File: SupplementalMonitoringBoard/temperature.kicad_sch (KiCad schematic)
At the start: 11 parts, among them U3 INA180B1

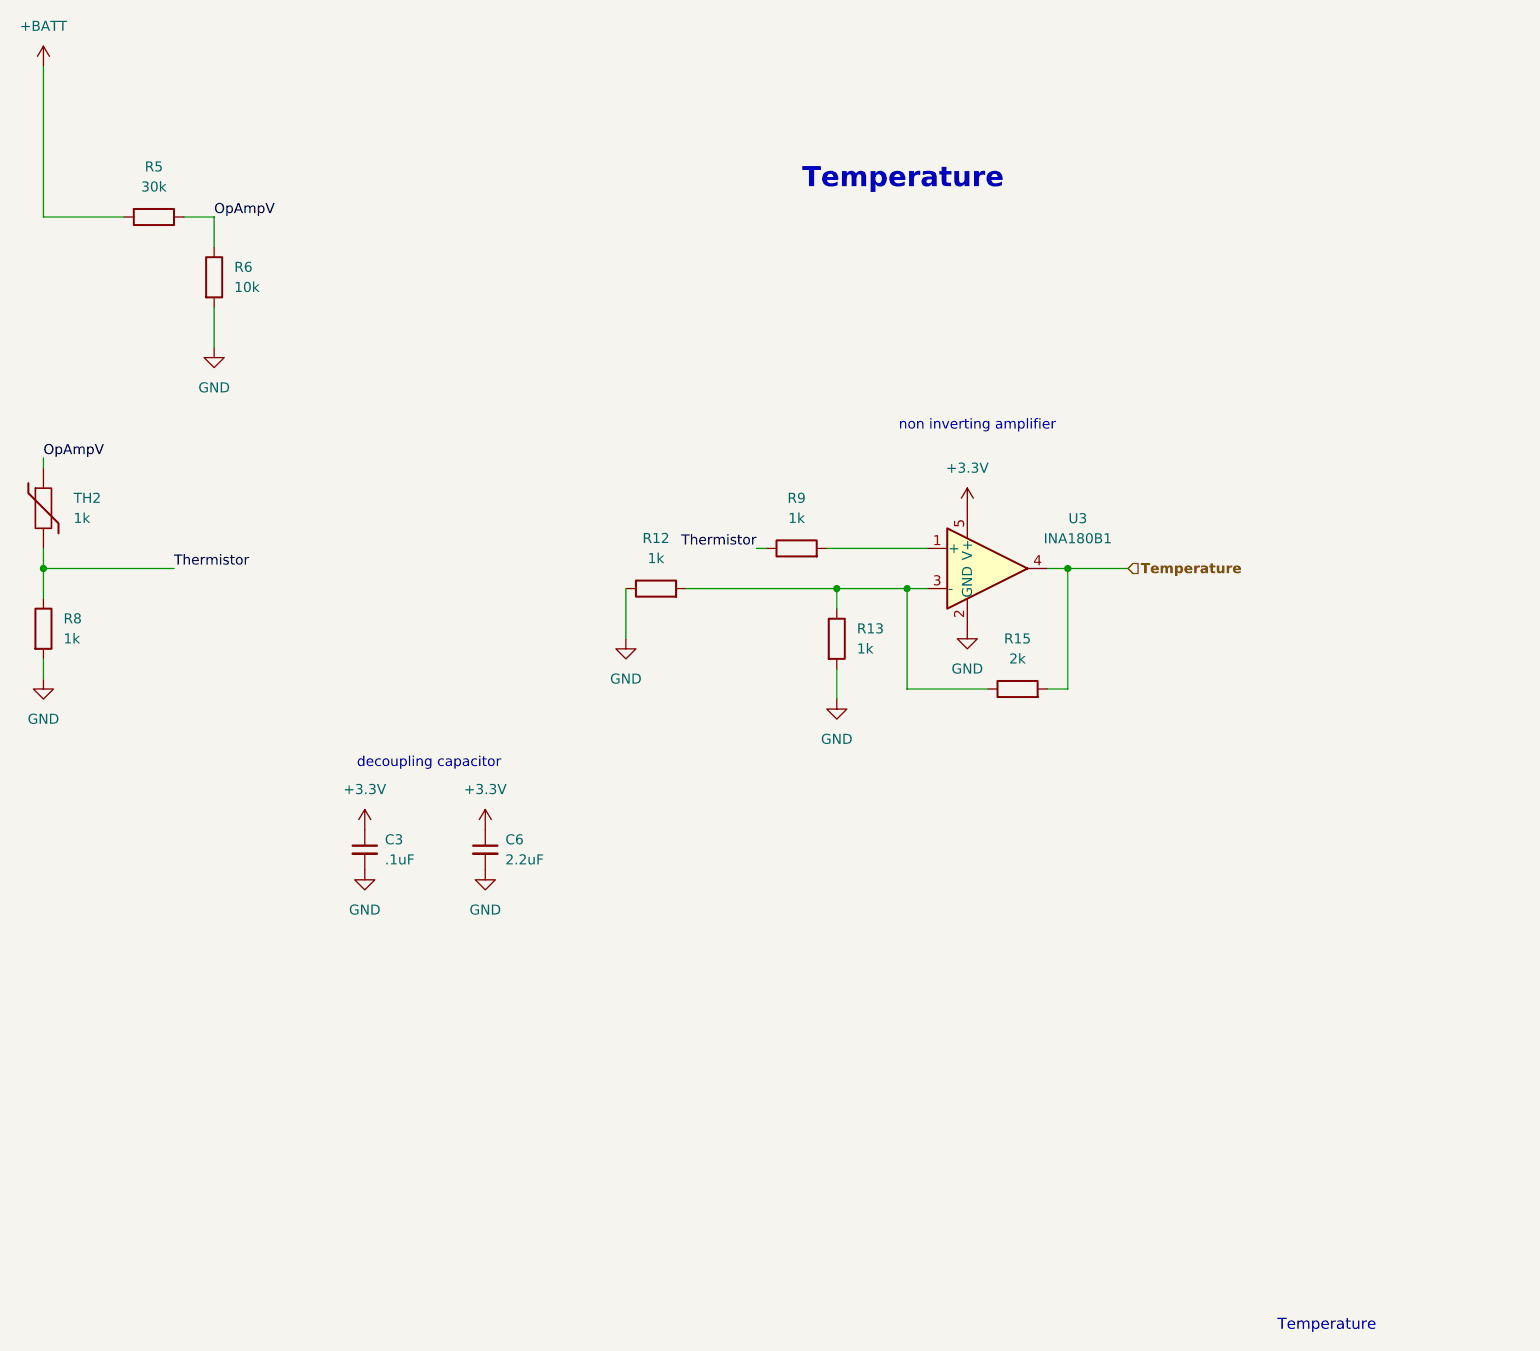
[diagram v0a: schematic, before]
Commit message: Supplemental Monitoring Board
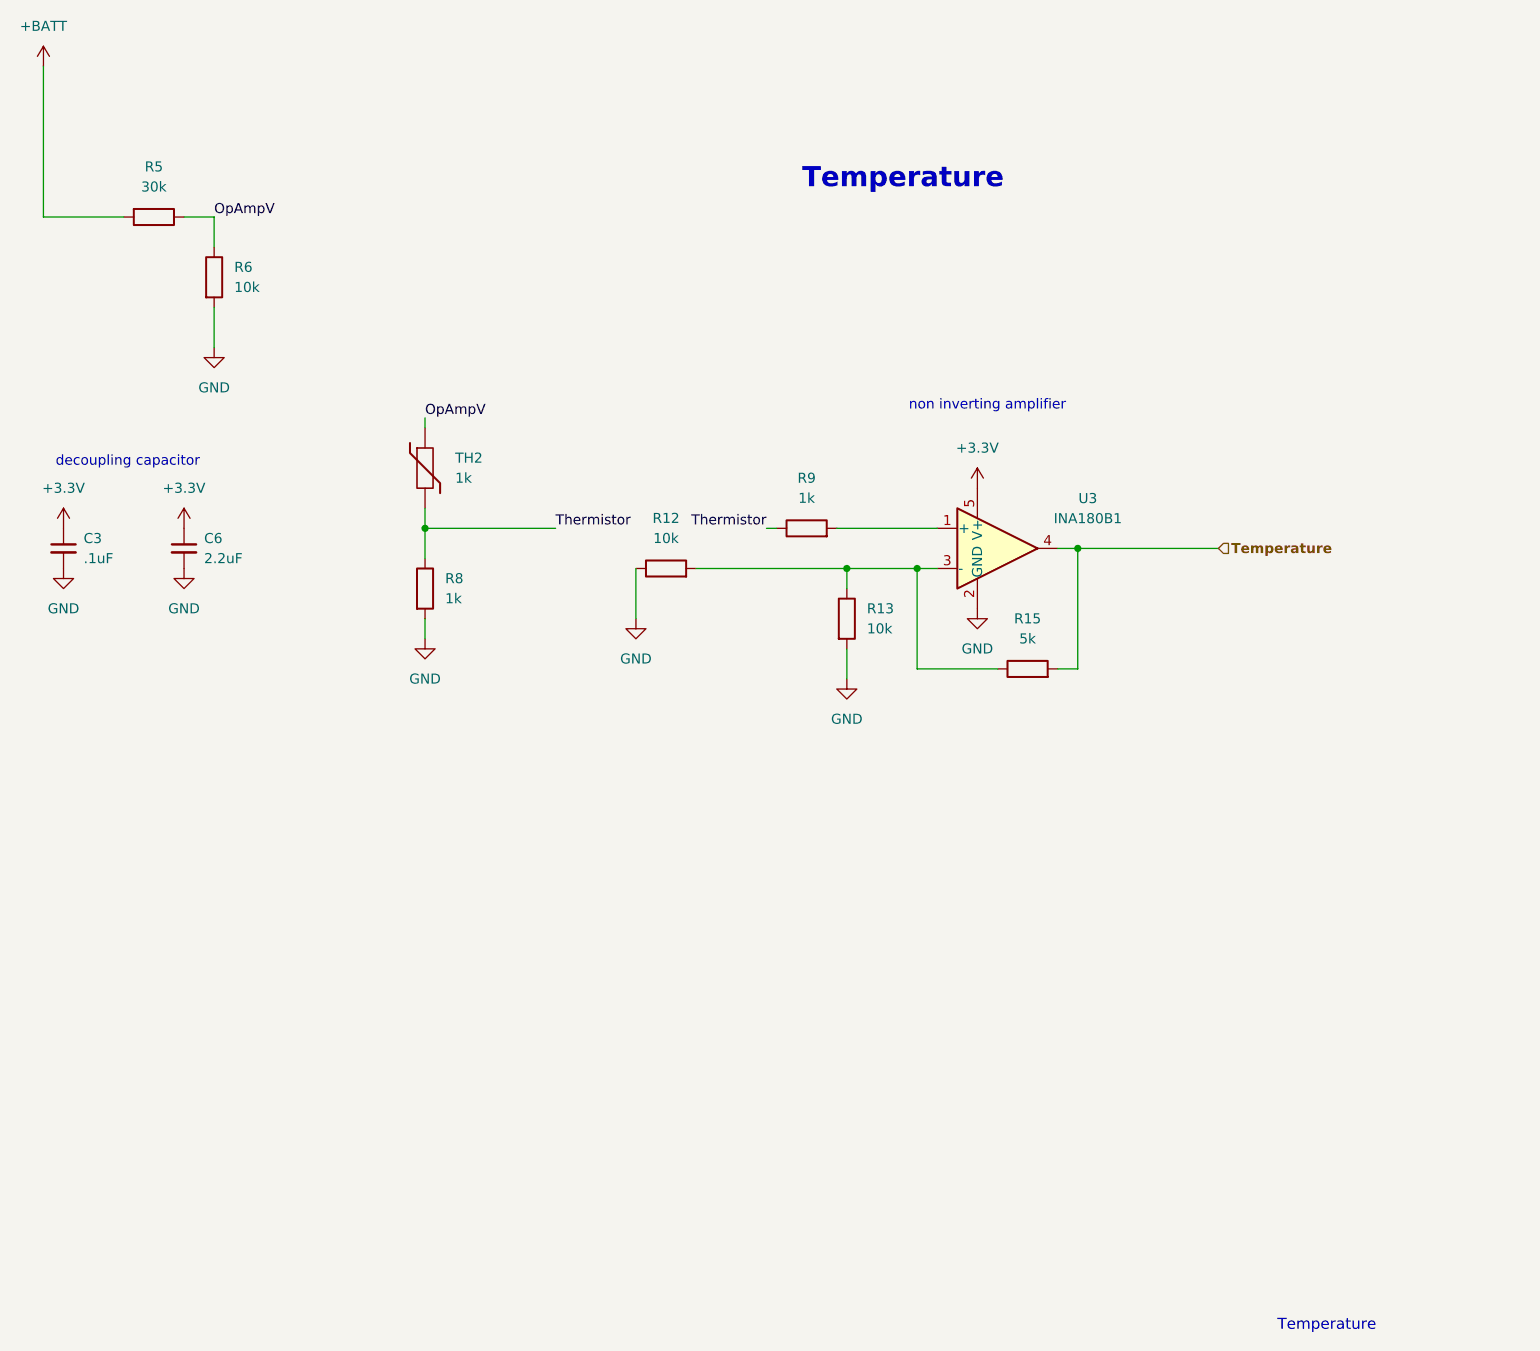
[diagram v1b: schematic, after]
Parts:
- R12, R13: value 1k -> 10k
- R15: value 2k -> 5k
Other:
- moved on the sheet: C3, C6, R12, R13, R15, R8, R9, TH2, U3

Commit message: Adressed Reviews - Supplemental Monitoring Board
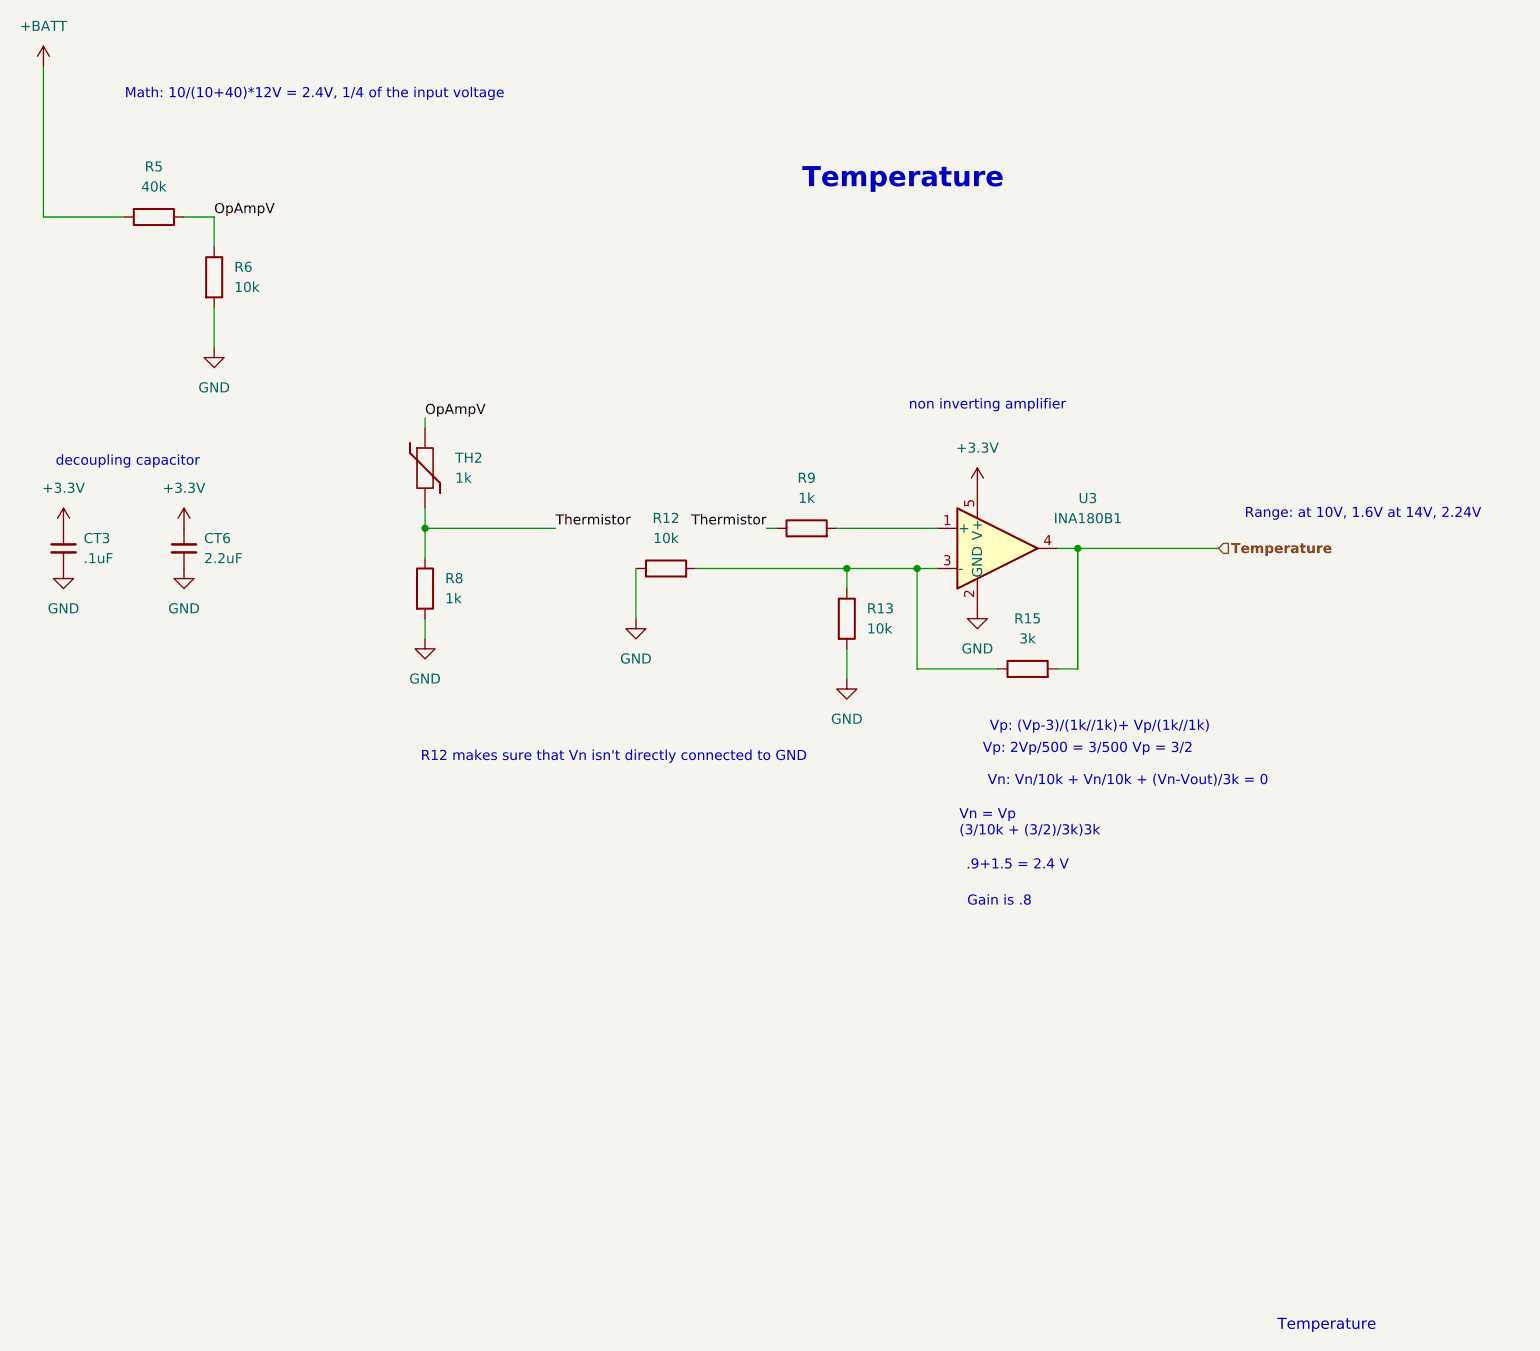
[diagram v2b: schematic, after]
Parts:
- R15: value 5k -> 3k
- R5: value 30k -> 40k
- renumbered C3 to CT3, C6 to CT6
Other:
- note added: ".9+1.5 = 2.4 V"
- note added: "Gain is .8"
- note added: "Math: 10/(10+40)*12V = 2.4V, 1/4 of the input voltage"
- note added: "R12 makes sure that Vn isn't directly connected to GND"
- note added: "Range: at 10V, 1.6V at 14V, 2.24V"
- note added: "Vn = Vp (3/10k + (3/2)/3k)3k"
- note added: "Vn: Vn/10k + Vn/10k + (Vn-Vout)/3k = 0"
- note added: "Vp: (Vp-3)/(1k//1k)+ Vp/(1k//1k)"
- note added: "Vp: 2Vp/500 = 3/500 Vp = 3/2"
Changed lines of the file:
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@@
+		)
+	)
+	(text "Vn = Vp\n(3/10k + (3/2)/3k)3k"
+		(exclude_from_sim no)
+		(at 147.574 126.238 0)
+		(effects
+			(font
+				(size 1.27 1.27)
+			)
+			(justify left)
 		)
 	)
@@
 		)
 	)
+	(text "Range: at 10V, 1.6V at 14V, 2.24V"
+		(exclude_from_sim no)
+		(at 198.628 87.122 0)
+		(effects
+			(font
+				(size 1.27 1.27)
+			)
+		)
+	)
+	(text ".9+1.5 = 2.4 V\n"
+		(exclude_from_sim no)
+		(at 154.94 131.572 0)
+		(effects
+			(font
+				(size 1.27 1.27)
+			)
+		)
+	)
+	(text "Vn: Vn/10k + Vn/10k + (Vn-Vout)/3k = 0"
+		(exclude_from_sim no)
+		(at 168.91 120.904 0)
+		(effects
+			(font
+				(size 1.27 1.27)
+			)
+		)
+	)
+	(text "Math: 10/(10+40)*12V = 2.4V, 1/4 of the input voltage\n"
+		(exclude_from_sim no)
+		(at 66.04 34.036 0)
+		(effects
+			(font
+				(size 1.27 1.27)
+			)
+		)
+	)
 	(text "decoupling capacitor"
 		(exclude_from_sim no)
@@
 				(size 1.27 1.27)
 				(thickness 0.1588)
+			)
+		)
+	)
+	(text "Vp: 2Vp/500 = 3/500 Vp = 3/2"
+		(exclude_from_sim no)
+		(at 163.83 116.84 0)
+		(effects
+			(font
+				(size 1.27 1.27)
 			)
 		)
@@
 				(thickness 0.1746)
 				(color 132 0 0 1)
+			)
+		)
+	)
+	(text "Vp: (Vp-3)/(1k//1k)+ Vp/(1k//1k)"
+		(exclude_from_sim no)
+		(at 165.354 114.046 0)
+		(effects
+			(font
+				(size 1.27 1.27)
+			)
+		)
+	)
+	(text "R12 makes sure that Vn isn't directly connected to GND\n"
+		(exclude_from_sim no)
+		(at 103.886 117.856 0)
+		(effects
+			(font
+				(size 1.27 1.27)
 			)
 		)
@@
 		)
 	)
+	(text "Gain is .8\n"
+		(exclude_from_sim no)
+		(at 152.654 136.144 0)
+		(effects
+			(font
+				(size 1.27 1.27)
+			)
+		)
+	)
 	(label "Thermistor"
 		(at 123.19 88.9 180)
@@
 		(dnp no)
 		(fields_autoplaced yes)
-		(property "Reference" "C6"
+		(property "Reference" "CT6"
 			(at 52.07 90.1762 0)
 			(effects
@@
 			(project "SupplementalMonitoringBoard"
 				(path "/aa0415d0-3287-4bc4-9a8e-766ada9ace2f/cde5a840-cd97-4154-b488-bad27326129c"
-					(reference "C6")
+					(reference "CT6")
 					(unit 1)
 				)
@@
 		(dnp no)
 		(fields_autoplaced yes)
-		(property "Reference" "C3"
+		(property "Reference" "CT3"
 			(at 36.83 90.1762 0)
 			(effects
@@
 			(project "SupplementalMonitoringBoard"
 				(path "/aa0415d0-3287-4bc4-9a8e-766ada9ace2f/cde5a840-cd97-4154-b488-bad27326129c"
-					(reference "C3")
+					(reference "CT3")
 					(unit 1)
 				)
@@
 			)
 		)
-		(property "Value" "30k"
+		(property "Value" "40k"
 			(at 45.72 45.72 90)
 			(effects
@@
 			)
 		)
-		(property "Value" "5k"
+		(property "Value" "3k"
 			(at 156.21 102.87 90)
 			(effects

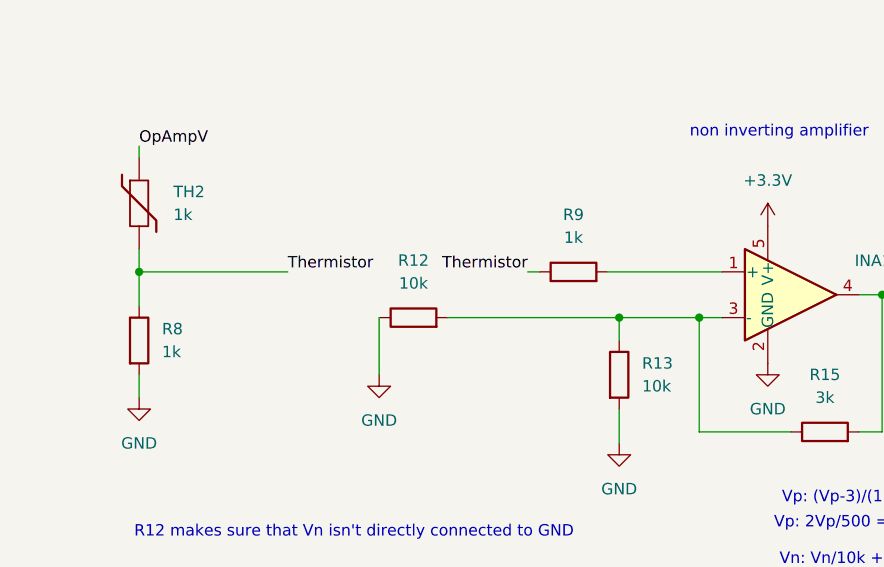
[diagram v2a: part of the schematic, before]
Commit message: PCB Layout - Supplemental Monitoring Board
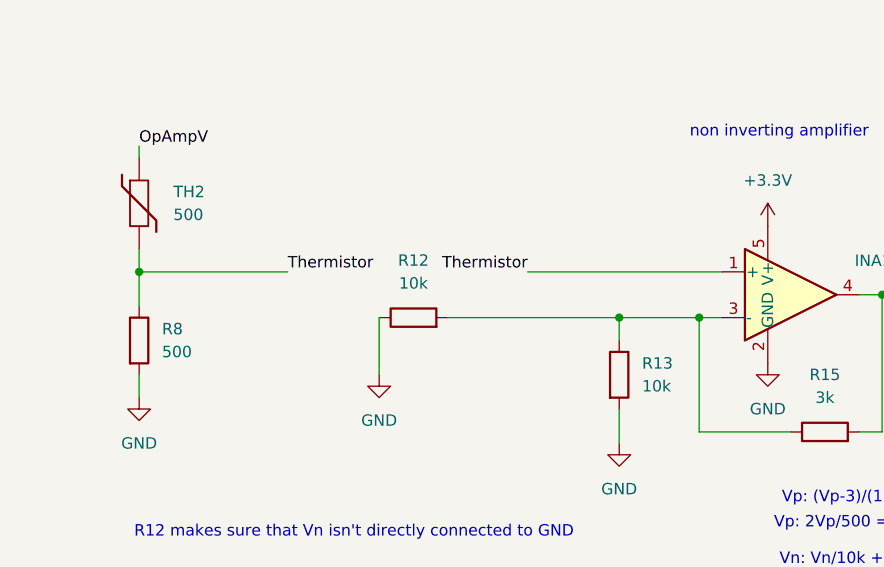
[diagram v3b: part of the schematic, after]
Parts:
- removed R9: 1k, Resistor_SMD:R_0805_2012Metric, symbol Device:R
- R8, TH2: value 1k -> 500
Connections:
- net Thermistor: now also U3.1 (+)
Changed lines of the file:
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@@
 	(wire
 		(pts
-			(xy 123.19 88.9) (xy 124.46 88.9)
-		)
-		(stroke
-			(width 0)
-			(type default)
-		)
-	)
-	(wire
-		(pts
-			(xy 132.08 88.9) (xy 144.78 88.9)
+			(xy 123.19 88.9) (xy 144.78 88.9)
 		)
 		(stroke
@@
 	(symbol
 		(lib_id "Device:R")
-		(at 128.27 88.9 90)
-		(unit 1)
-		(exclude_from_sim no)
-		(in_bom yes)
-		(on_board yes)
-		(dnp no)
-		(property "Reference" "R9"
-			(at 128.27 82.55 90)
-			(effects
-				(font
-					(size 1.27 1.27)
-				)
-			)
-		)
-		(property "Value" "1k"
-			(at 128.27 85.09 90)
-			(effects
-				(font
-					(size 1.27 1.27)
-				)
-			)
-		)
-		(property "Footprint" "Resistor_SMD:R_0805_2012Metric"
-			(at 128.27 90.678 90)
-			(effects
-				(font
-					(size 1.27 1.27)
-				)
-				(hide yes)
-			)
-		)
-		(property "Datasheet" "~"
-			(at 128.27 88.9 0)
-			(effects
-				(font
-					(size 1.27 1.27)
-				)
-				(hide yes)
-			)
-		)
-		(property "Description" "Resistor"
-			(at 128.27 88.9 0)
-			(effects
-				(font
-					(size 1.27 1.27)
-				)
-				(hide yes)
-			)
-		)
-		(pin "1"
-		)
-		(pin "2"
-		)
-		(instances
-			(project "SupplementalMonitoringBoard"
-				(path "/aa0415d0-3287-4bc4-9a8e-766ada9ace2f/cde5a840-cd97-4154-b488-bad27326129c"
-					(reference "R9")
-					(unit 1)
-				)
-			)
-		)
-	)
-	(symbol
-		(lib_id "Device:R")
 		(at 53.34 57.15 0)
 		(unit 1)
@@
 			)
 		)
-		(property "Value" "1k"
+		(property "Value" "500"
 			(at 83.82 82.5499 0)
 			(effects
@@
 			)
 		)
-		(property "Value" "1k"
+		(property "Value" "500"
 			(at 82.55 97.7899 0)
 			(effects
